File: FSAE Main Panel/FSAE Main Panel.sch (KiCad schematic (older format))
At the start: 15 parts, among them J101 Conn_01x06, U1 SAMD21G18A-AU, Y1 32.768kHz

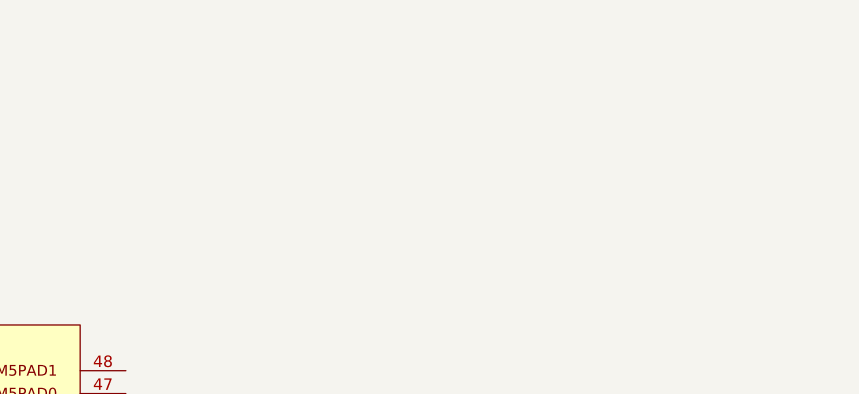
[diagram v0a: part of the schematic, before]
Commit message: Finished most LEDs, begun power regulators
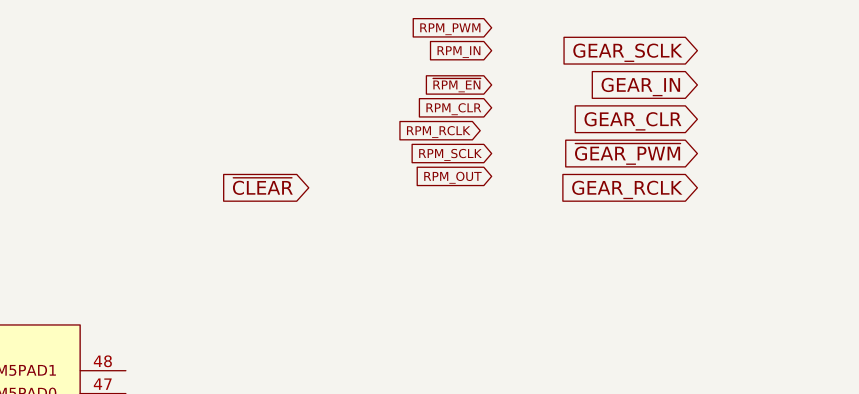
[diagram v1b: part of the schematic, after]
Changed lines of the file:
@@
 Wire Wire Line
 	7200 2900 7050 2900
+Text GLabel 7850 1300 0    60   Input ~ 0
+~CLEAR
+Text GLabel 8650 850  0    39   Input ~ 0
+~RPM_EN
+Text GLabel 8650 950  0    39   Input ~ 0
+RPM_CLR
+Text GLabel 8650 700  0    39   Input ~ 0
+RPM_IN
+Text GLabel 8650 1150 0    39   Input ~ 0
+RPM_SCLK
+Text GLabel 8600 1050 0    39   Input ~ 0
+RPM_RCLK
+Text GLabel 8650 1250 0    39   Input ~ 0
+RPM_OUT
+Text GLabel 9550 1150 0    60   Input ~ 0
+~GEAR_PWM
+Text GLabel 9550 1000 0    60   Input ~ 0
+GEAR_CLR
+Text GLabel 9550 1300 0    60   Input ~ 0
+GEAR_RCLK
+Text GLabel 9550 700  0    60   Input ~ 0
+GEAR_SCLK
+Text GLabel 9550 850  0    60   Input ~ 0
+GEAR_IN
+Text GLabel 8650 600  0    39   Input ~ 0
+RPM_PWM
 $EndSCHEMATC

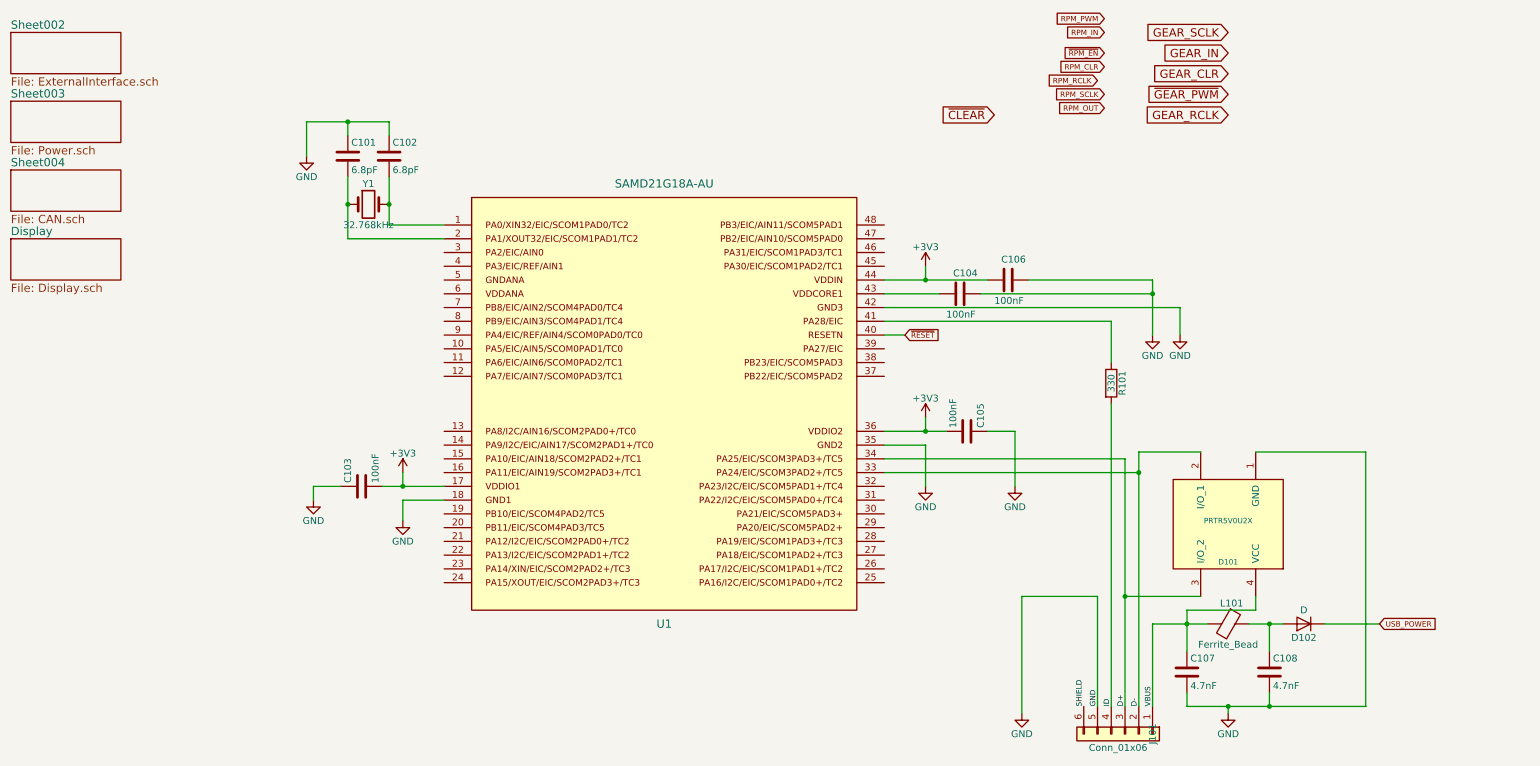
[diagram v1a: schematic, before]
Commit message: Moved USB connection to External_Interface
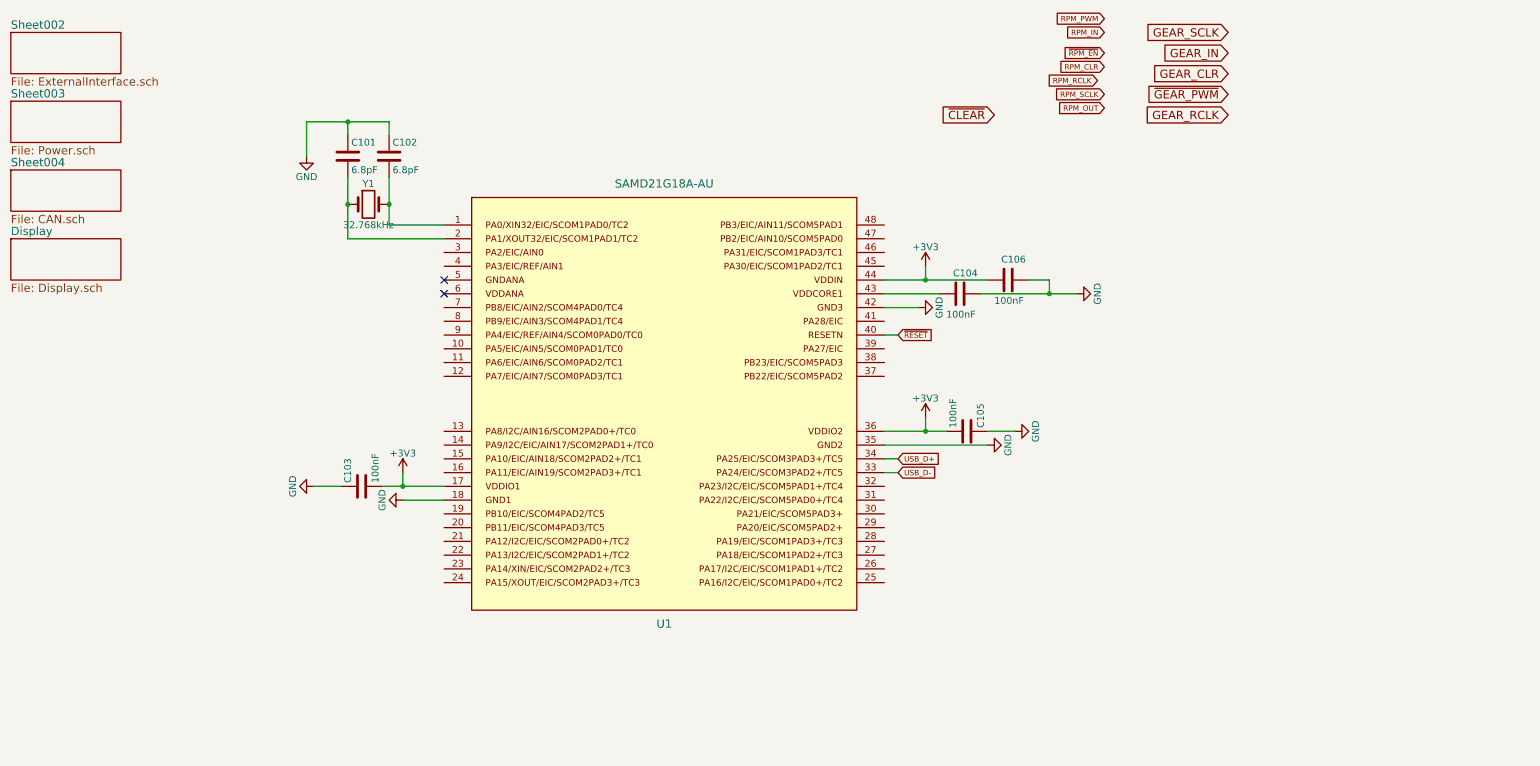
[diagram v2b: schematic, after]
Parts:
- removed C107, C108: 4.7nF, symbol C
- removed D101: PRTR5V0U2X, symbol PRTR5V0U2X
- removed D102: D, symbol D
- removed J101: Conn_01x06, symbol Conn_01x06
- removed L101: Ferrite_Bead, symbol Ferrite_Bead
- removed R101: 330, symbol R
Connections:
- net D+ renamed USB_D+
- net D- renamed USB_D-
- no-connect marks 0 -> 2

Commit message: Updated power circuit for MCU, used small components on main sheet
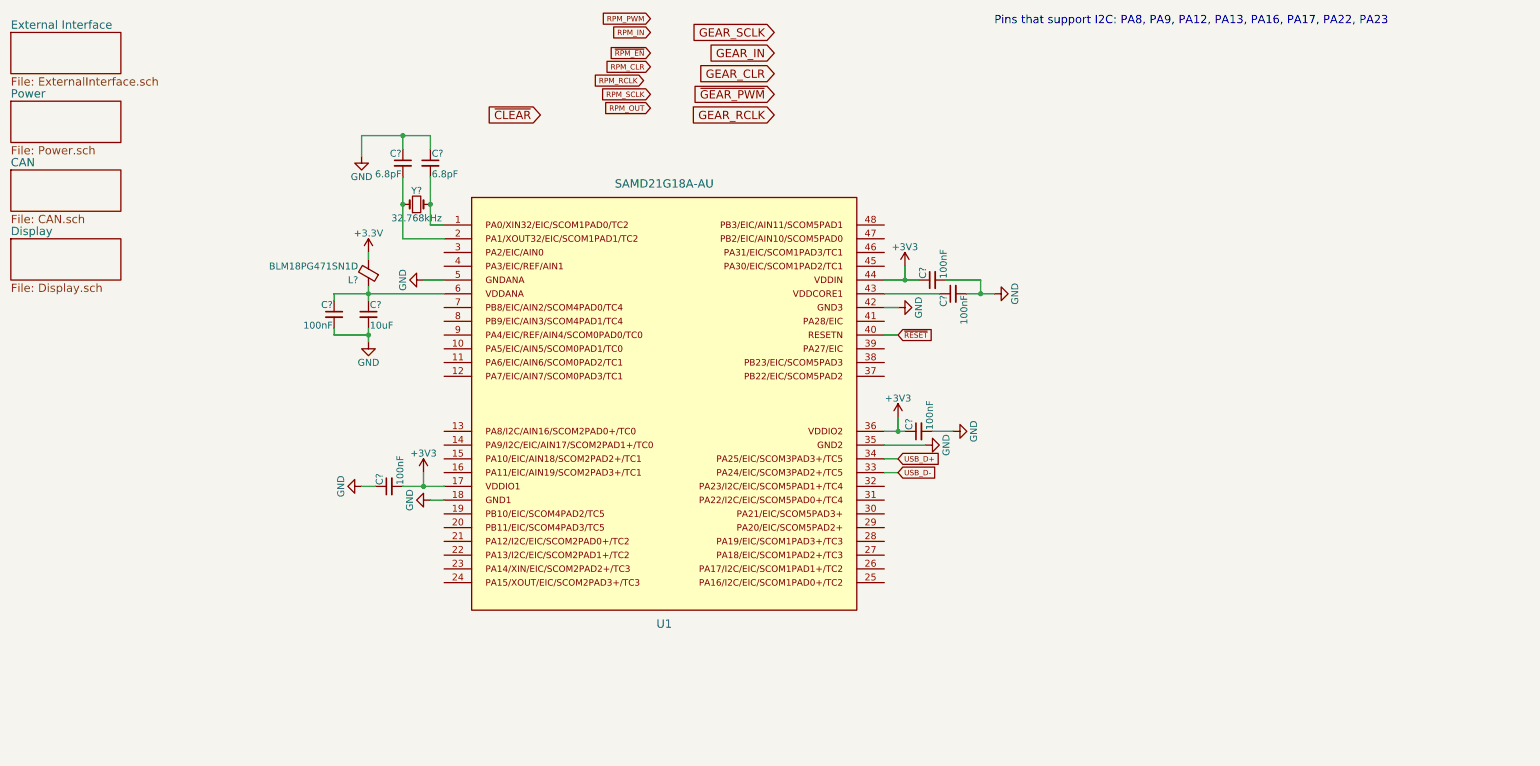
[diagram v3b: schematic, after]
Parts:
- removed C101, C102: 6.8pF, symbol C
- removed C103, C104, C105, C106: 100nF, symbol C
- removed Y1: 32.768kHz, symbol Crystal
- added C?: 10uF, symbol C_Small
- added C? (x5): 100nF, symbol C_Small
- added C? (x2): 6.8pF, symbol C_Small
- added L?: BLM18PG471SN1D, symbol Ferrite_Bead_Small
- added Y?: 32.768kHz, symbol Crystal_Small
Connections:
- net +3V3: now also C?.1, C?.1, C?.2, L?.2
- net GND: now also U1.5, C?.1, C?.1, C?.1, C?.2, C?.2, C?.2, C?.2, C?.2
- net at U1.1: now also C?.2, Y?.2
- net at U1.2: now also C?.2, Y?.1
- net at U1.43: now also C?.1
- net at U1.6: now also C?.1, C?.1, L?.1
- no-connect marks 2 -> 0
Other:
- note added: "Pins that support I2C: PA8, PA9, PA12, PA13, PA16, PA17, PA22, PA23"

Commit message: Cortex debugger, GPIO pinning, minor fixes
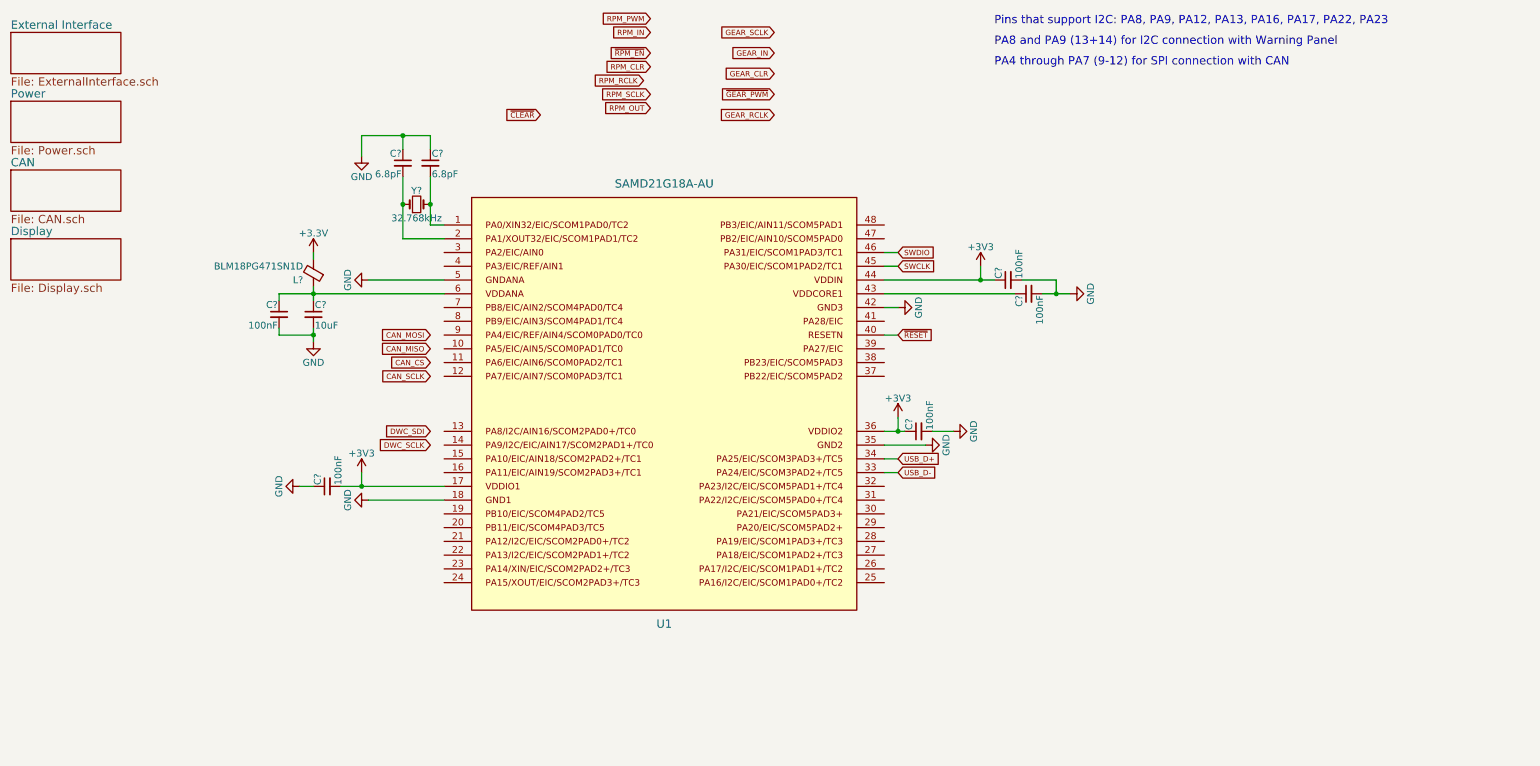
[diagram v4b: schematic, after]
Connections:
- net SWCLK: now reaches U1.45
- net SWDIO: now reaches U1.46
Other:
- note added: "PA4 through PA7 (9-12) for SPI connection with CAN"
- note added: "PA8 and PA9 (13+14) for I2C connection with Warning Panel"
- moved on the sheet: C?, L?

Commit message: Added power regulator for LEDs, further GPIO considerations
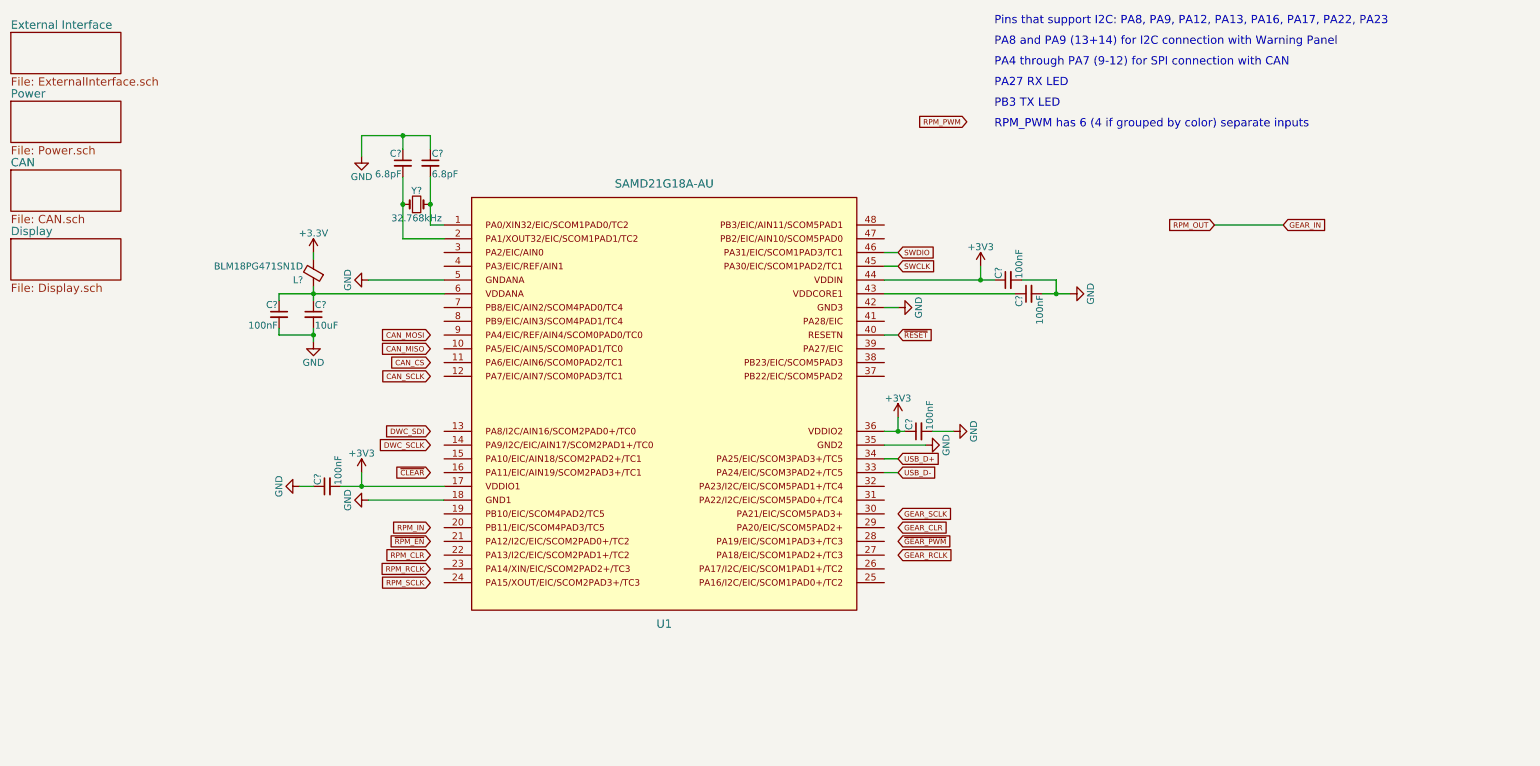
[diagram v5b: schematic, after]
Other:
- note added: "PA27 RX LED"
- note added: "PB3 TX LED"
- note added: "RPM_PWM has 6 (4 if grouped by color) separate inputs"
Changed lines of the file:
@@
 $EndComp
 Wire Wire Line
-	3250 1450 3750 1450
+	3250 1450 3550 1450
+Wire Wire Line
+	3550 1450 3750 1450
 Wire Wire Line
 	3250 1450 3250 1600
@@
 Connection ~ 3550 1950
 Wire Wire Line
-	3750 1750 3750 2100
-Wire Wire Line
-	3550 1750 3550 2200
+	3750 1750 3750 1950
+Wire Wire Line
+	3750 1950 3750 2100
+Wire Wire Line
+	3550 1750 3550 1950
+Wire Wire Line
+	3550 1950 3550 2200
 Wire Wire Line
 	3550 1550 3550 1450
@@
 	7750 2500 7750 2400
 Wire Wire Line
-	7050 2500 7850 2500
+	7050 2500 7750 2500
+Wire Wire Line
+	7750 2500 7850 2500
 Wire Wire Line
 	7150 3600 7150 3500
 Wire Wire Line
-	7050 3600 7200 3600
+	7050 3600 7150 3600
+Wire Wire Line
+	7150 3600 7200 3600
 Wire Wire Line
 	3250 3900 3250 4000
 Wire Wire Line
-	3100 4000 3850 4000
+	3100 4000 3250 4000
+Wire Wire Line
+	3250 4000 3850 4000
 $Comp
 L GND #PWR108
@@
 	7050 2600 8000 2600
 Wire Wire Line
-	8200 2600 8400 2600
+	8200 2600 8300 2600
+Wire Wire Line
+	8300 2600 8400 2600
 Connection ~ 8300 2600
 Connection ~ 7150 3600
@@
 Wire Wire Line
 	7150 2900 7050 2900
-Text GLabel 4550 1300 0    39   Input ~ 0
+Text GLabel 3750 3900 0    39   Input ~ 0
 ~CLEAR
-Text GLabel 5350 850  0    39   Input ~ 0
+Text GLabel 3750 4400 0    39   Input ~ 0
 ~RPM_EN
-Text GLabel 5350 950  0    39   Input ~ 0
+Text GLabel 3750 4500 0    39   Input ~ 0
 RPM_CLR
-Text GLabel 5350 700  0    39   Input ~ 0
+Text GLabel 3750 4300 0    39   Input ~ 0
 RPM_IN
-Text GLabel 5350 1150 0    39   Input ~ 0
+Text GLabel 3750 4700 0    39   Input ~ 0
 RPM_SCLK
-Text GLabel 5300 1050 0    39   Input ~ 0
+Text GLabel 3750 4600 0    39   Input ~ 0
 RPM_RCLK
-Text GLabel 5350 1250 0    39   Input ~ 0
+Text GLabel 9450 2100 0    39   Input ~ 0
 RPM_OUT
-Text GLabel 6250 1150 0    39   Input ~ 0
+Text GLabel 7150 4400 2    39   Input ~ 0
 ~GEAR_PWM
-Text GLabel 6250 1000 0    39   Input ~ 0
+Text GLabel 7150 4300 2    39   Input ~ 0
 GEAR_CLR
-Text GLabel 6250 1300 0    39   Input ~ 0
+Text GLabel 7150 4500 2    39   Input ~ 0
 GEAR_RCLK
-Text GLabel 6250 700  0    39   Input ~ 0
+Text GLabel 7150 4200 2    39   Input ~ 0
 GEAR_SCLK
-Text GLabel 6250 850  0    39   Input ~ 0
+Text GLabel 9950 2100 2    39   Input ~ 0
 GEAR_IN
-Text GLabel 5350 600  0    39   Input ~ 0
+Text GLabel 7650 1350 0    39   Input ~ 0
 RPM_PWM
 Text GLabel 7150 3800 2    39   Input ~ 0
@@
 	2900 2300 2900 2350
 Wire Wire Line
-	2900 2550 2900 2650
-Wire Wire Line
-	2650 2600 3850 2600
+	2900 2550 2900 2600
+Wire Wire Line
+	2900 2600 2900 2650
+Wire Wire Line
+	2650 2600 2900 2600
+Wire Wire Line
+	2900 2600 3850 2600
 Connection ~ 2900 2600
 $Comp
@@
 	2650 2900 2900 2900
 Wire Wire Line
-	2900 2850 2900 2950
+	2900 2850 2900 2900
+Wire Wire Line
+	2900 2900 2900 2950
 Connection ~ 2900 2900
 $Comp
@@
 Text GLabel 3750 3700 0    39   Input ~ 0
 DWC_SCLK
+Text Notes 7850 1100 0    60   ~ 0
+PA27 RX LED
+Text Notes 7850 1250 0    60   ~ 0
+PB3 TX LED
+Wire Wire Line
+	9950 2100 9450 2100
+Text Notes 7850 1400 0    60   ~ 0
+RPM_PWM has 6 (4 if grouped by color) separate inputs
 $EndSCHEMATC

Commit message: Updated to KiCad 5
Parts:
- C101, C102, C103, C104, C105, C106, C107, C108: renamed from C?; symbol C_Small -> Device:C_Small
- L101: renamed from L?; symbol Ferrite_Bead_Small -> Device:Ferrite_Bead_Small
- U1: symbol SAMD21G18A-AU -> samd21g18a-au:SAMD21G18A-AU
- Y101: renamed from Y?; symbol Crystal_Small -> Device:Crystal_Small
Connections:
- net CAN_CS: now also U1.11
- net CAN_MISO: now also U1.10
- net CAN_MOSI: now also U1.9
- net CAN_SCLK: now also U1.12
- net DWC_SCLK: now also U1.14
- net DWC_SDI: now also U1.13
- net GEAR_CLR: now also U1.29
- net GEAR_RCLK: now also U1.27
- net GEAR_SCLK: now also U1.30
- net RPM_CLR: now also U1.22
- net RPM_IN: now also U1.20
- net RPM_RCLK: now also U1.23
- net RPM_SCLK: now also U1.24
- net ~CLEAR: now also U1.16
- net ~GEAR_PWM: now also U1.28
- net ~RPM_EN: now also U1.21
